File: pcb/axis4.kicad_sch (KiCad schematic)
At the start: 7 parts, among them J14 Mini v1.0 / 15-hole socket, J24 MOTOR PHASES male 1x3, J34 ENCODER breakout FEMALE 1x6

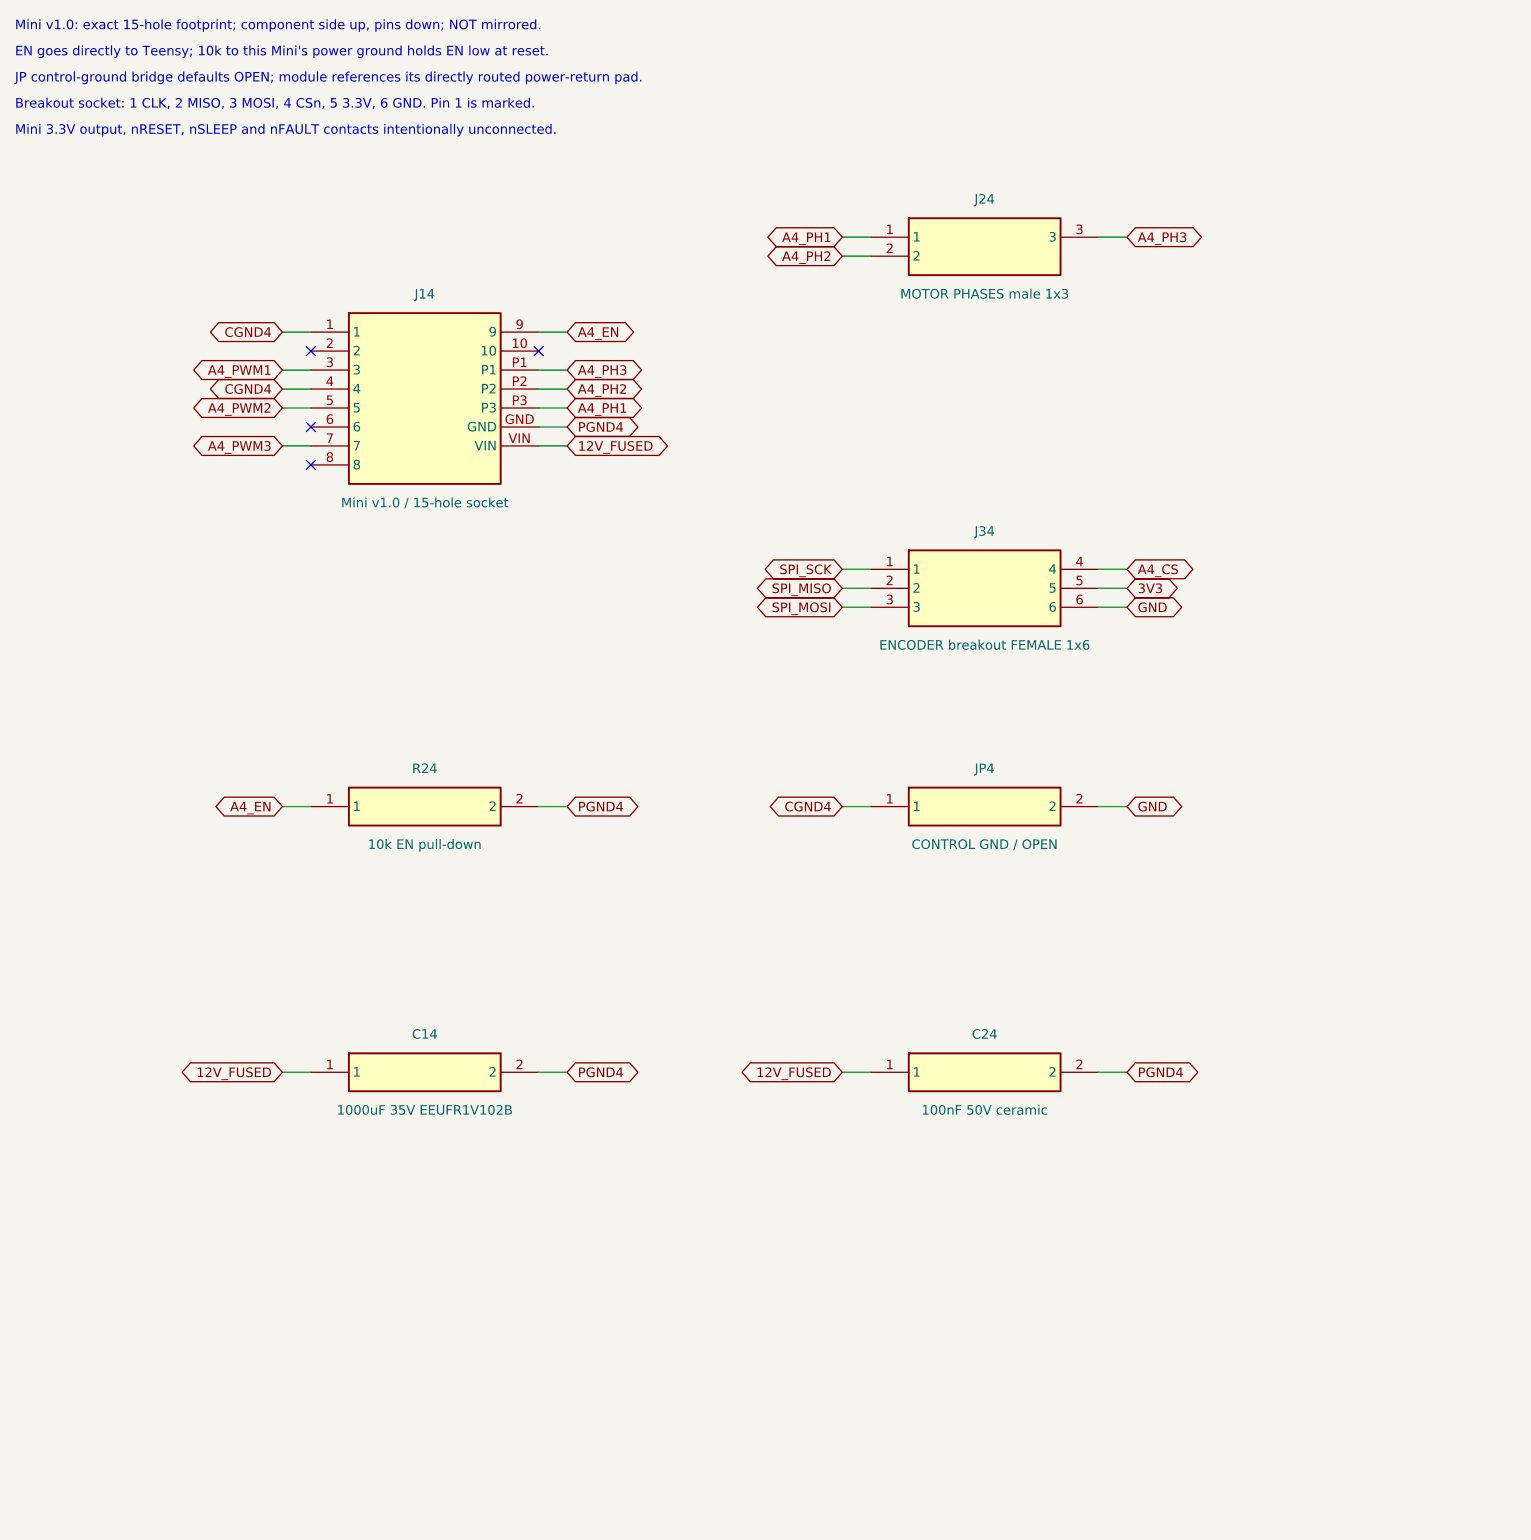
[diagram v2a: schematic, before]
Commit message: feat: relayout carrier with edge connectors and hardware kill
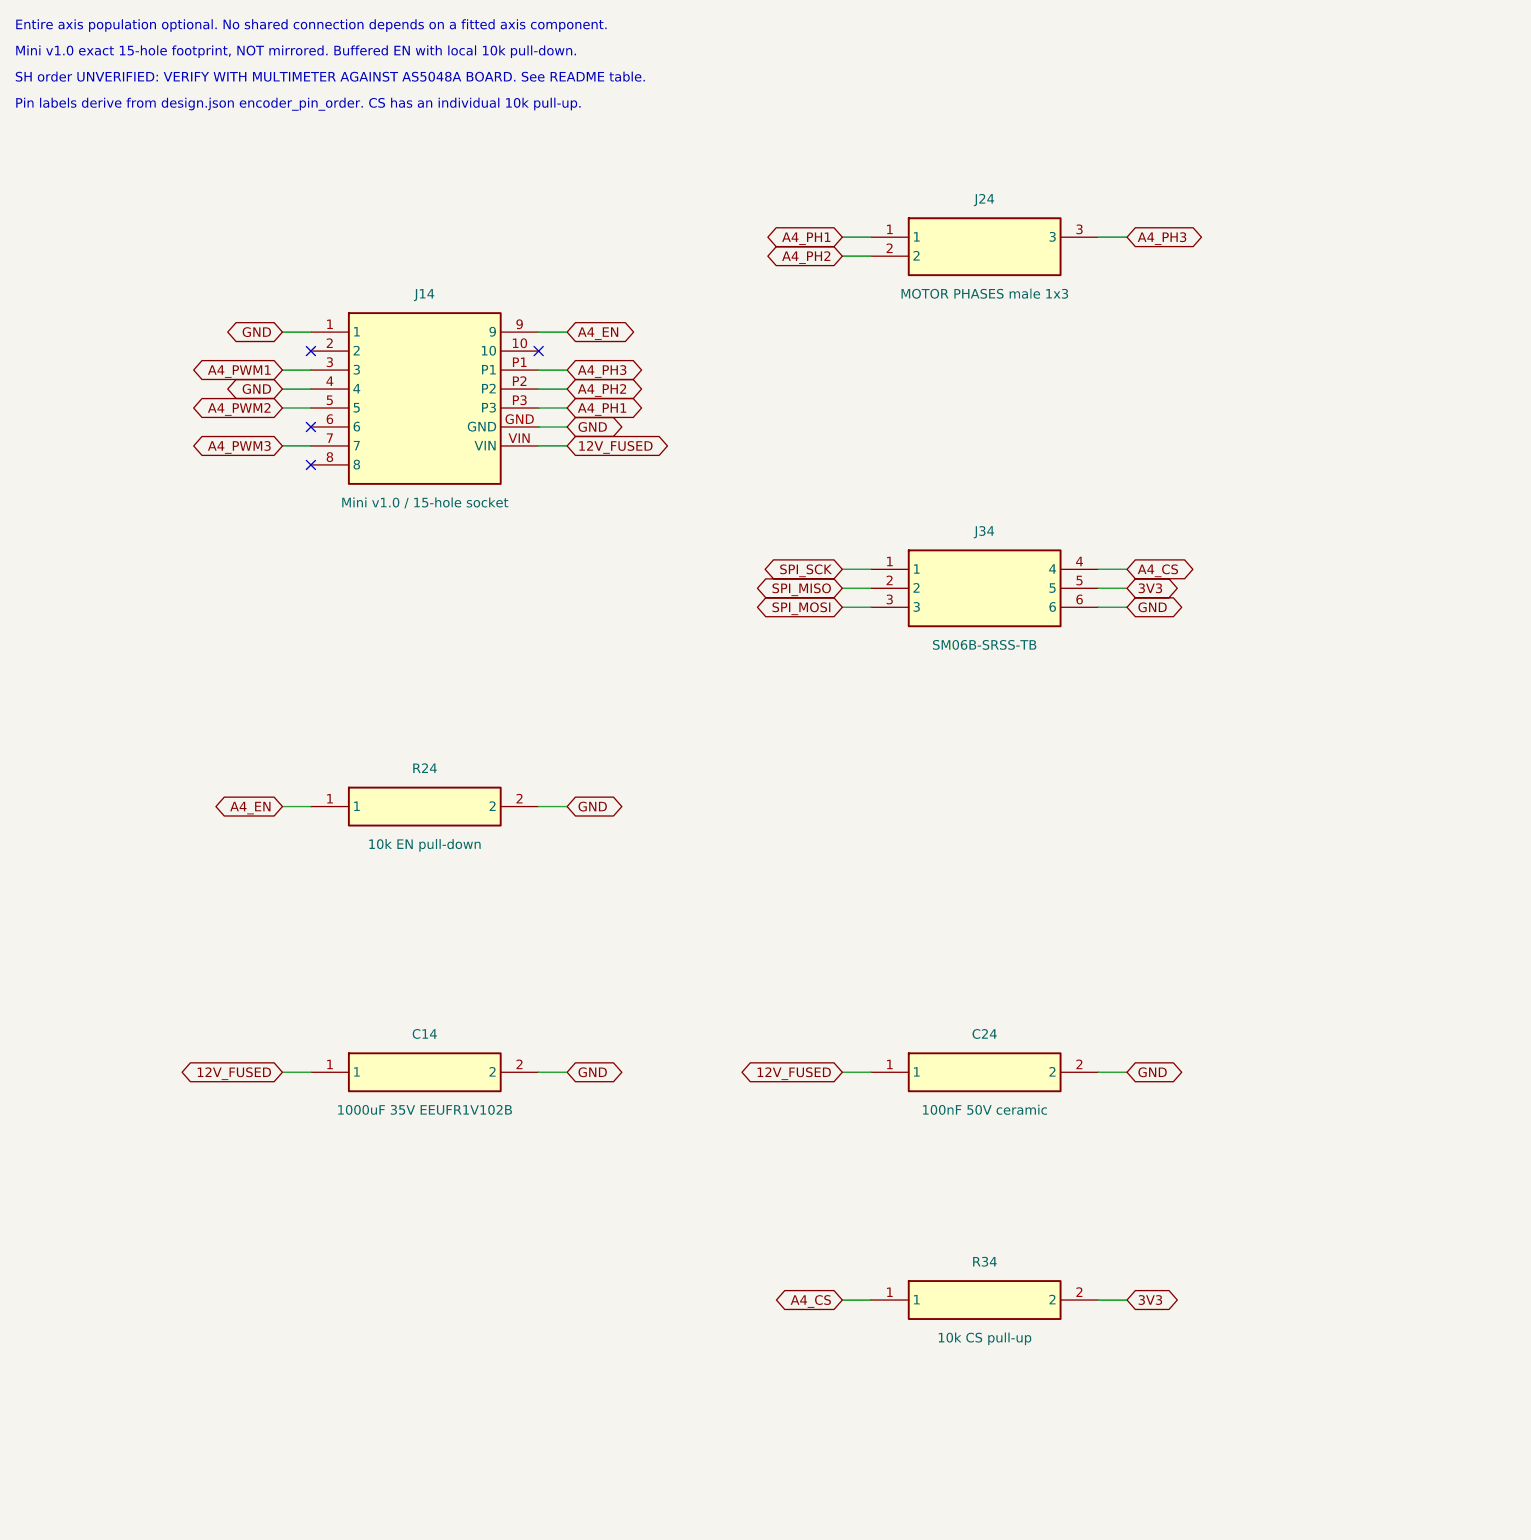
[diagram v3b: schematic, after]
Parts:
- removed JP4: CONTROL GND / OPEN, TrueSkate:GroundBridge_THT, symbol TrueSkate:JP4
- added R34: 10k CS pull-up, TrueSkate:Edge_R_Axial_DIN0207_L6.3mm_D2.5mm_P7.62mm_Horizontal, symbol TrueSkate:R34
- C14: footprint Capacitor_THT:CP_Radial_D12.5mm_P5.00mm -> TrueSkate:Edge_CP_Radial_D12.5mm_P5.00mm
- C24: footprint Capacitor_THT:C_Disc_D5.0mm_W2.5mm_P5.00mm -> TrueSkate:Edge_C_Disc_D5.0mm_W2.5mm_P5.00mm
- J24: footprint Connector_PinHeader_2.54mm:PinHeader_1x03_P2.54mm_Vertical -> TrueSkate:Edge_PinHeader_1x03_P2.54mm_Vertical
- J34: value ENCODER breakout FEMALE 1x6 -> SM06B-SRSS-TB; footprint Connector_PinSocket_2.54mm:PinSocket_1x06_P2.54mm_Vertical -> TrueSkate:Edge_JST_SH_SM06B-SRSS-TB_1x06-1MP_P1.00mm_Horizontal
- R24: footprint Resistor_THT:R_Axial_DIN0207_L6.3mm_D2.5mm_P7.62mm_Horizontal -> TrueSkate:Edge_R_Axial_DIN0207_L6.3mm_D2.5mm_P7.62mm_Horizontal
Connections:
- net CGND4 is gone; now on net GND: J14.1, J14.4
- net PGND4 is gone; now on net GND: C14.2, C24.2, J14.GND, R24.2
- net 3V3: now also R34.2
- net A4_CS: now also R34.1
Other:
- note added: "Entire axis population optional. No shared connection depends on a fitted axis component."
- note added: "Mini v1.0 exact 15-hole footprint, NOT mirrored. Buffered EN with local 10k pull-down."
- note added: "Pin labels derive from design.json encoder_pin_order. CS has an individual 10k pull-up."
- note added: "SH order UNVERIFIED: VERIFY WITH MULTIMETER AGAINST AS5048A BOARD. See README table."
- note removed: "Breakout socket: 1 CLK, 2 MISO, 3 MOSI, 4 CSn, 5 3.3V, 6 GND. Pin 1 is marked."
- note removed: "EN goes directly to Teensy; 10k to this Mini's power ground holds EN low at reset."
- note removed: "JP control-ground bridge defaults OPEN; module references its directly routed power-return pad."
- note removed: "Mini 3.3V output, nRESET, nSLEEP and nFAULT contacts intentionally unconnected."
- note removed: "Mini v1.0: exact 15-hole footprint; component side up, pins down; NOT mirrored."
